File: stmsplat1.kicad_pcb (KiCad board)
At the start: 2 copper layers, 5 parts, among them CN10 Conn_01x34_Male, CN7 Conn_01x20_Male, CN8 Conn_01x16_Male, CN9 Conn_01x30_Male, U1 NUCLEO144-F746ZG

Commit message: Experimented with KiCad operations
Tried new symbols  / footprints etc
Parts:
- added J1: Conn_Coaxial, Connector_Coaxial:SMB_Jack_Vertical, F.Cu at (61.6, 49.5)
- added J2: Conn_Coaxial, Connector_Coaxial:SMB_Jack_Vertical, F.Cu at (93.3, 59.1)
- added J3: Conn_Coaxial, Connector_Coaxial:SMB_Jack_Vertical, F.Cu at (93.3, 38.1)
- added RN1: R_Pack04, Resistor_SMD:R_Array_Convex_4x1206, F.Cu at (73.4, 61.3)
- added RN2: R_Pack04, Resistor_SMD:R_Array_Convex_4x1206, F.Cu at (82.5, 61.3)
- added U2: SA630D, Package_SO:SOIC-8_3.9x4.9mm_P1.27mm, F.Cu at (81.9, 48.9)

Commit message: minor changes - still experimenting
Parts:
- added CN1: C_Pack04, symbols:C_Array_Convex_4x1206, F.Cu at (111.8, 49.5)
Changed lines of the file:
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@@
     (tracks 0)
     (zones 0)
-    (modules 11)
-    (nets 272)
+    (modules 12)
+    (nets 280)
   )
   (page A4)
@@
   (net 270 "Net-(RN2-Pad4)")
   (net 271 "Net-(RN2-Pad1)")
+  (net 272 "Net-(CN1-Pad1)")
+  (net 273 "Net-(CN1-Pad4)")
+  (net 274 "Net-(CN1-Pad2)")
+  (net 275 "Net-(CN1-Pad3)")
+  (net 276 "Net-(CN1-Pad7)")
+  (net 277 "Net-(CN1-Pad8)")
+  (net 278 "Net-(CN1-Pad5)")
+  (net 279 "Net-(CN1-Pad6)")
   (net_class Default "This is the default net class."
     (clearance 0.2)
@@
     (uvia_dia 0.3)
     (uvia_drill 0.1)
+    (add_net "Net-(CN1-Pad1)")
+    (add_net "Net-(CN1-Pad2)")
+    (add_net "Net-(CN1-Pad3)")
+    (add_net "Net-(CN1-Pad4)")
+    (add_net "Net-(CN1-Pad5)")
+    (add_net "Net-(CN1-Pad6)")
+    (add_net "Net-(CN1-Pad7)")
+    (add_net "Net-(CN1-Pad8)")
     (add_net "Net-(CN10-Pad1)")
     (add_net "Net-(CN10-Pad10)")
@@
     (add_net "Net-(U2-Pad7)")
   )
+  (module symbols:C_Array_Convex_4x1206 (layer F.Cu)
+    (at 111.76 49.53)
+    (descr "Chip Resistor Network, ROHM MNR34 (see mnr_g.pdf)")
+    (tags "resistor array")
+    (attr smd)
+    (fp_text reference CN1 (at 0 -3.5) (layer F.SilkS)
+      (effects (font (size 1 1) (thickness 0.15)))
+    )
+    (fp_text value C_Pack04 (at 0 3.5) (layer F.Fab)
+      (effects (font (size 1 1) (thickness 0.15)))
+    )
+    (fp_text user %R (at 0 0 90) (layer F.Fab)
+      (effects (font (size 0.7 0.7) (thickness 0.105)))
+    )
+    (fp_line (start -1.6 -2.6) (end -1.6 2.6) (layer F.Fab) (width 0.1))
+    (fp_line (start -1.6 2.6) (end 1.6 2.6) (layer F.Fab) (width 0.1))
+    (fp_line (start 1.6 2.6) (end 1.6 -2.6) (layer F.Fab) (width 0.1))
+    (fp_line (start 1.6 -2.6) (end -1.6 -2.6) (layer F.Fab) (width 0.1))
+    (fp_line (start 1.05 2.67) (end -1.05 2.67) (layer F.SilkS) (width 0.12))
+    (fp_line (start 1.05 -2.67) (end -1.05 -2.67) (layer F.SilkS) (width 0.12))
+    (fp_line (start -2.21 -2.85) (end 2.2 -2.85) (layer F.CrtYd) (width 0.05))
+    (fp_line (start -2.21 -2.85) (end -2.21 2.85) (layer F.CrtYd) (width 0.05))
+    (fp_line (start 2.2 2.85) (end 2.2 -2.85) (layer F.CrtYd) (width 0.05))
+    (fp_line (start 2.2 2.85) (end -2.21 2.85) (layer F.CrtYd) (width 0.05))
+    (pad 1 smd rect (at -1.5 -2) (size 0.9 0.9) (layers F.Cu F.Paste F.Mask)
+      (net 272 "Net-(CN1-Pad1)"))
+    (pad 4 smd rect (at -1.5 2) (size 0.9 0.9) (layers F.Cu F.Paste F.Mask)
+      (net 273 "Net-(CN1-Pad4)"))
+    (pad 2 smd rect (at -1.5 -0.66) (size 0.9 0.9) (layers F.Cu F.Paste F.Mask)
+      (net 274 "Net-(CN1-Pad2)"))
+    (pad 3 smd rect (at -1.5 0.66) (size 0.9 0.9) (layers F.Cu F.Paste F.Mask)
+      (net 275 "Net-(CN1-Pad3)"))
+    (pad 7 smd rect (at 1.5 -0.66) (size 0.9 0.9) (layers F.Cu F.Paste F.Mask)
+      (net 276 "Net-(CN1-Pad7)"))
+    (pad 8 smd rect (at 1.5 -2) (size 0.9 0.9) (layers F.Cu F.Paste F.Mask)
+      (net 277 "Net-(CN1-Pad8)"))
+    (pad 5 smd rect (at 1.5 2) (size 0.9 0.9) (layers F.Cu F.Paste F.Mask)
+      (net 278 "Net-(CN1-Pad5)"))
+    (pad 6 smd rect (at 1.5 0.66) (size 0.9 0.9) (layers F.Cu F.Paste F.Mask)
+      (net 279 "Net-(CN1-Pad6)"))
+    (model ${KISYS3DMOD}/Resistor_SMD.3dshapes/R_Array_Convex_4x1206.wrl
+      (at (xyz 0 0 0))
+      (scale (xyz 1 1 1))
+      (rotate (xyz 0 0 0))
+    )
+  )
   (module Resistor_SMD:R_Array_Convex_4x1206 (layer F.Cu)

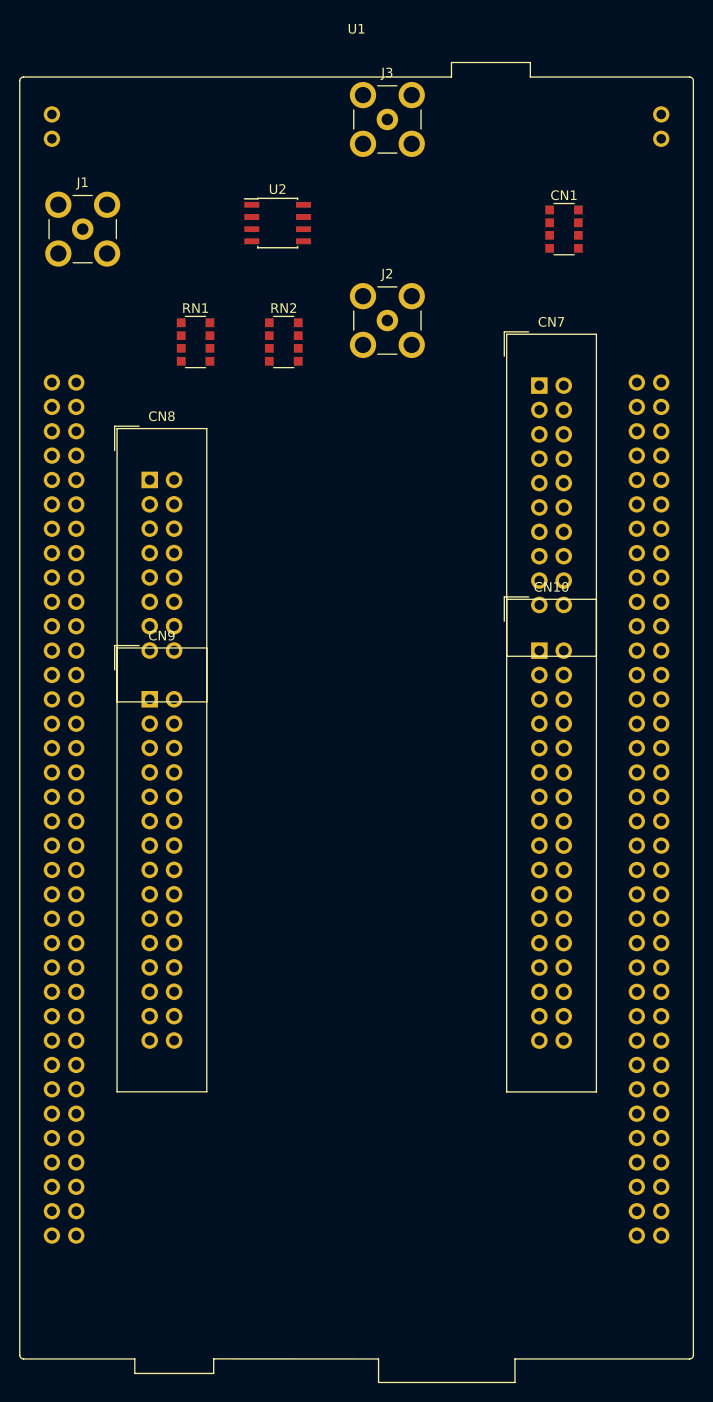
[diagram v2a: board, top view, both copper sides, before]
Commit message: pcb outline and start trim of connectors
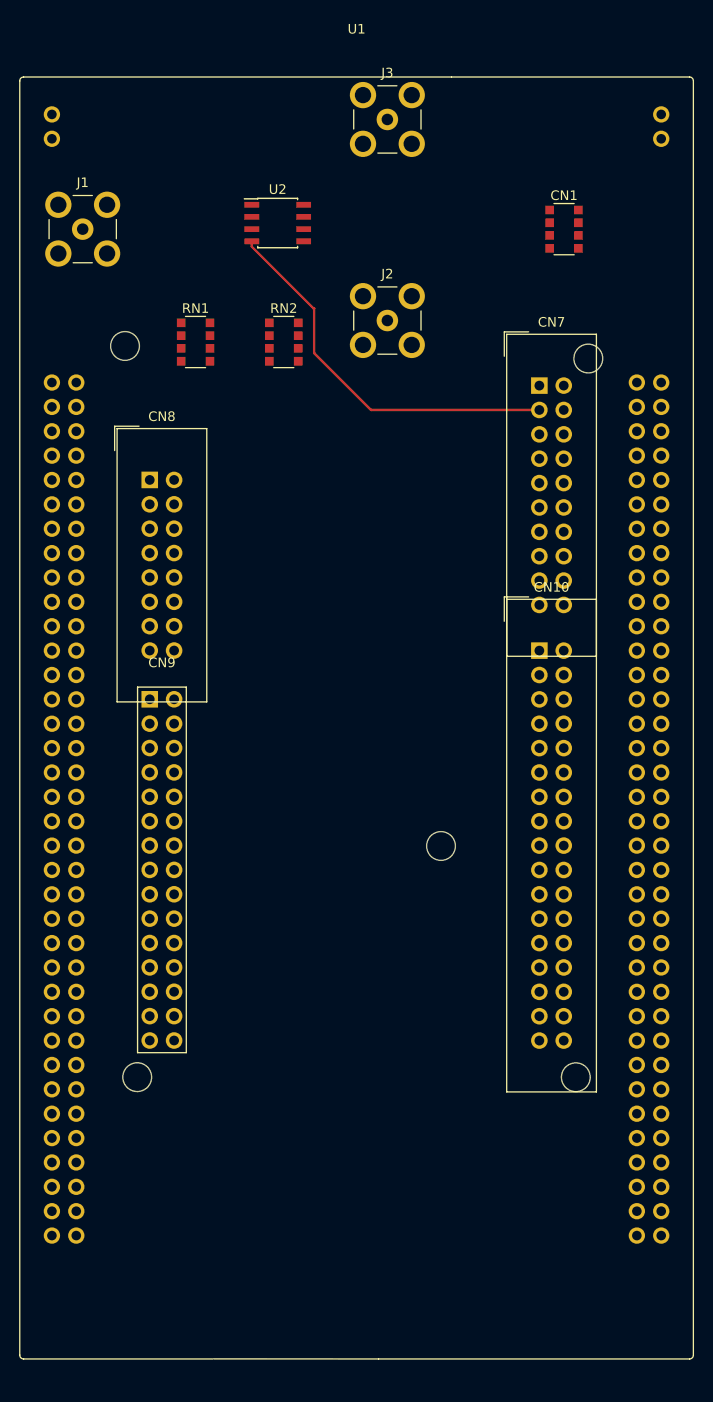
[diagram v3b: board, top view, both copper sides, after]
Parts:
- CN9: footprint Connector_IDC:IDC-Header_2x15_P2.54mm_Vertical -> symbols:IDC-Pins_2x15_P2.54mm_Vertical
- U1: footprint Module:ST_Morpho_Connector_144_STLink -> symbols:ST_Nucleo_144_Large_Daughter
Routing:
- net /PB15: track 0.00 -> 40.3 mm

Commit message: Getting ready for proper start to project
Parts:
- added U3: MCP6S93-X_UN, spatboard:MCP6S93-X&slash_UN, F.Cu at (95.9, 48.3)
- CN1: value C_Pack04 -> C_Pack04-c_pack04; footprint symbols:C_Array_Convex_4x1206 -> spatboard:C_Array_Convex_5x1206
- CN10: footprint Connector_IDC:IDC-Header_2x17_P2.54mm_Vertical -> spatboard:IDC-Pins_2x17_P2.54mm_Vertical
- CN7: footprint Connector_IDC:IDC-Header_2x10_P2.54mm_Vertical -> spatboard:IDC-Pins_2x10_P2.54mm_Vertical
- CN8: footprint Connector_IDC:IDC-Header_2x08_P2.54mm_Vertical -> spatboard:IDC-Pins_2x8_P2.54mm_Vertical
- U2: value SA630D -> SA630D-RF_Switch

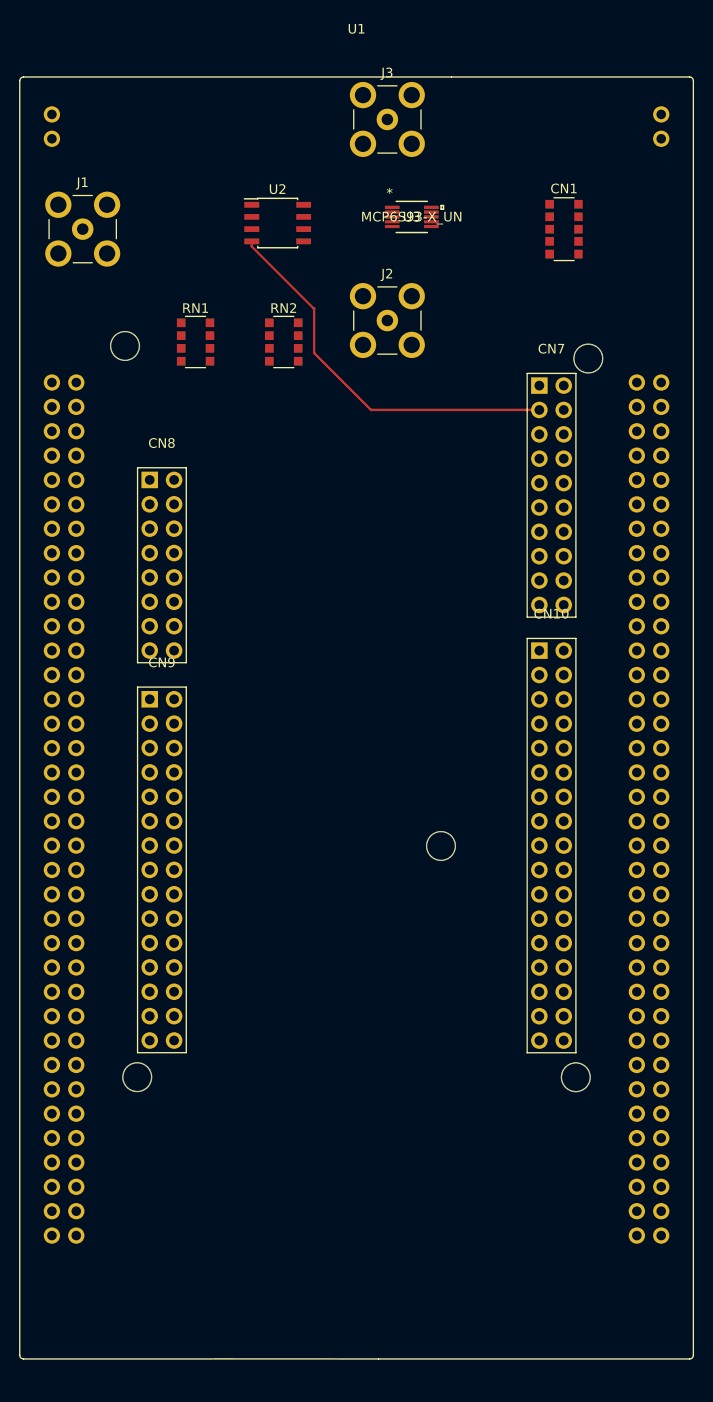
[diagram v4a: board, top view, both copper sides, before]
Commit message: Arduino connectors moved to correct position
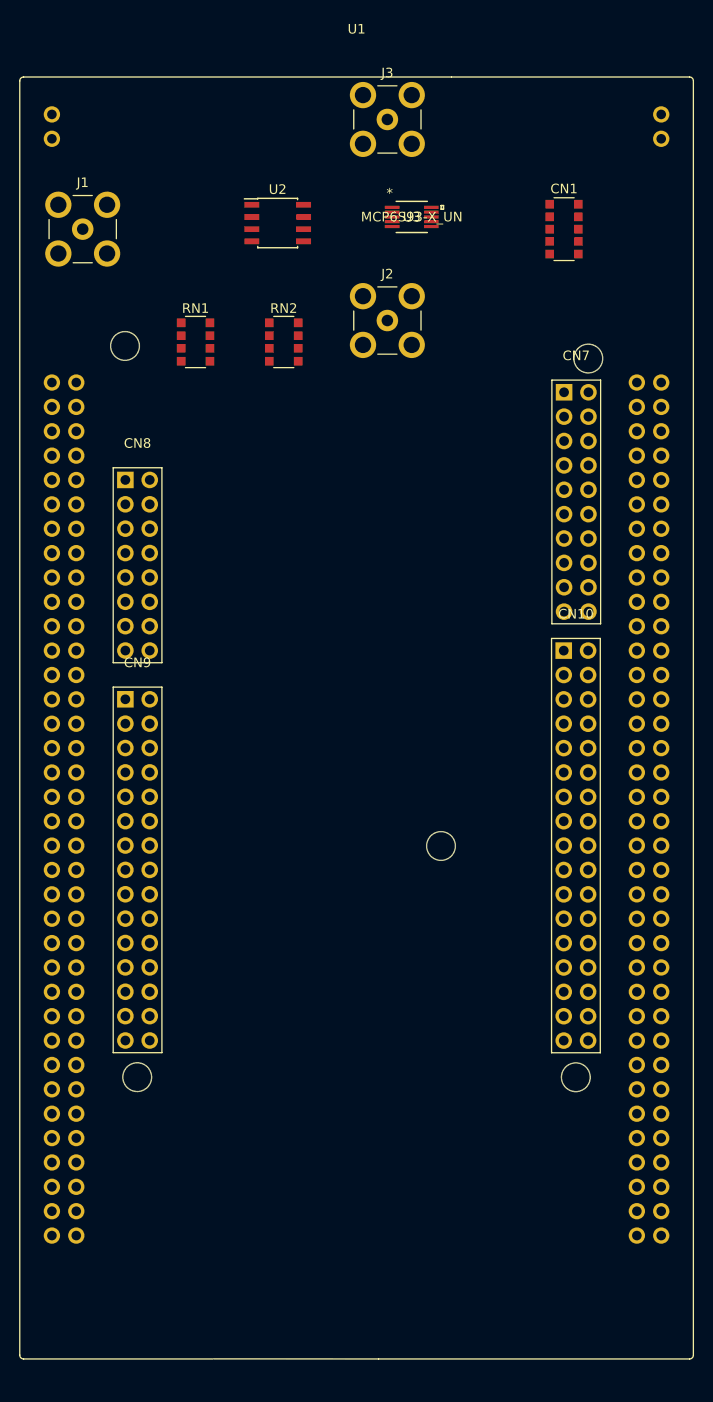
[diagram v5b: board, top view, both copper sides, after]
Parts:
- moved CN7 2.67 mm to (111.8, 66.5)
- moved CN10 2.54 mm to (111.7, 93.5)
- moved CN8 2.54 mm to (66.0, 75.7)
- moved CN9 2.54 mm to (66.0, 98.5)
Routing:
- net /PB15: track 40.3 -> 0.00 mm

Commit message: Cropped PCB to clear STM board buttons
Added GPS module connector and silkscreen
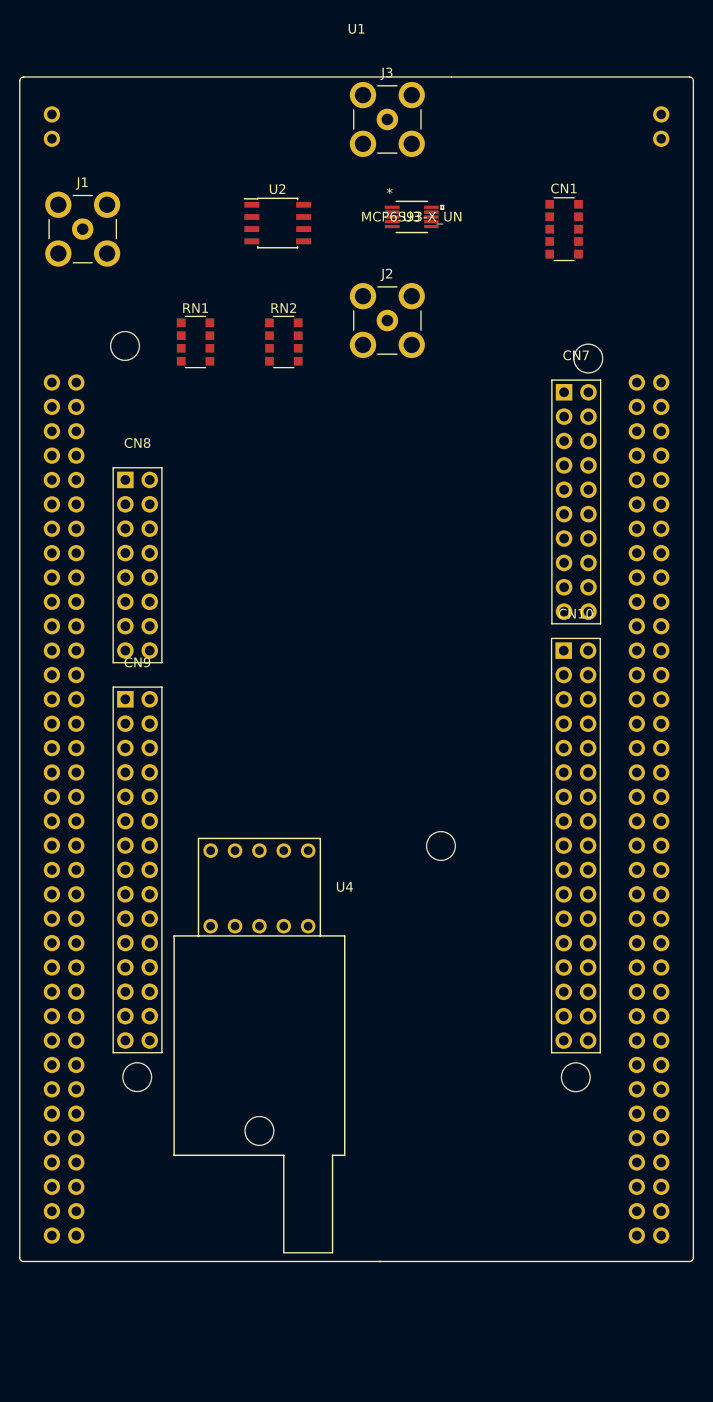
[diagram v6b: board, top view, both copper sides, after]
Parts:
- added U4: ublox_SAM-M8Q, spatboard:GPS_IDC-Header_2x05_P2.54mm_Horizontal, F.Cu at (85.1, 114.3)
- CN9: footprint symbols:IDC-Pins_2x15_P2.54mm_Vertical -> spatboard:IDC-Pins_2x15_P2.54mm_Vertical
- U1: footprint symbols:ST_Nucleo_144_Large_Daughter -> spatboard:ST_Nucleo_144_Large_Daughter

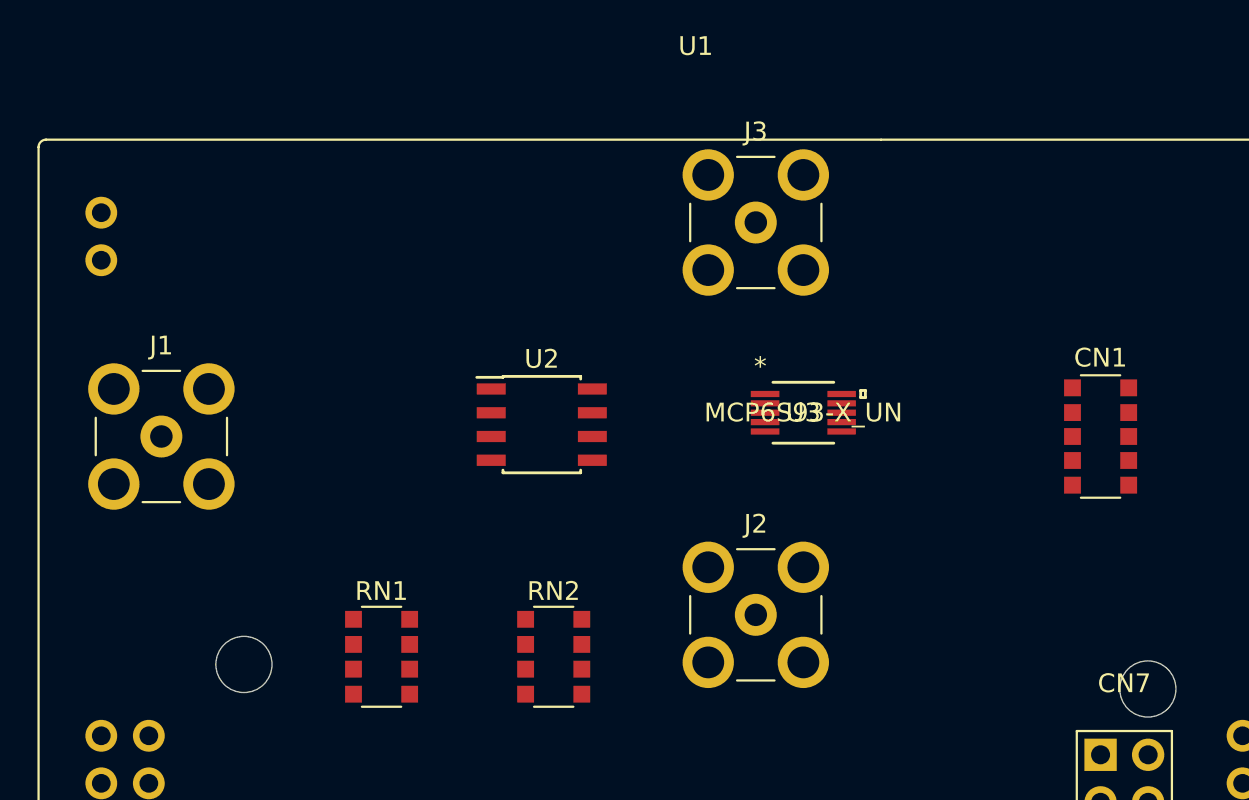
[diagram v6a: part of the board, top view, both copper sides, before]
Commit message: Footprints re-assigned
PCB had lost associations
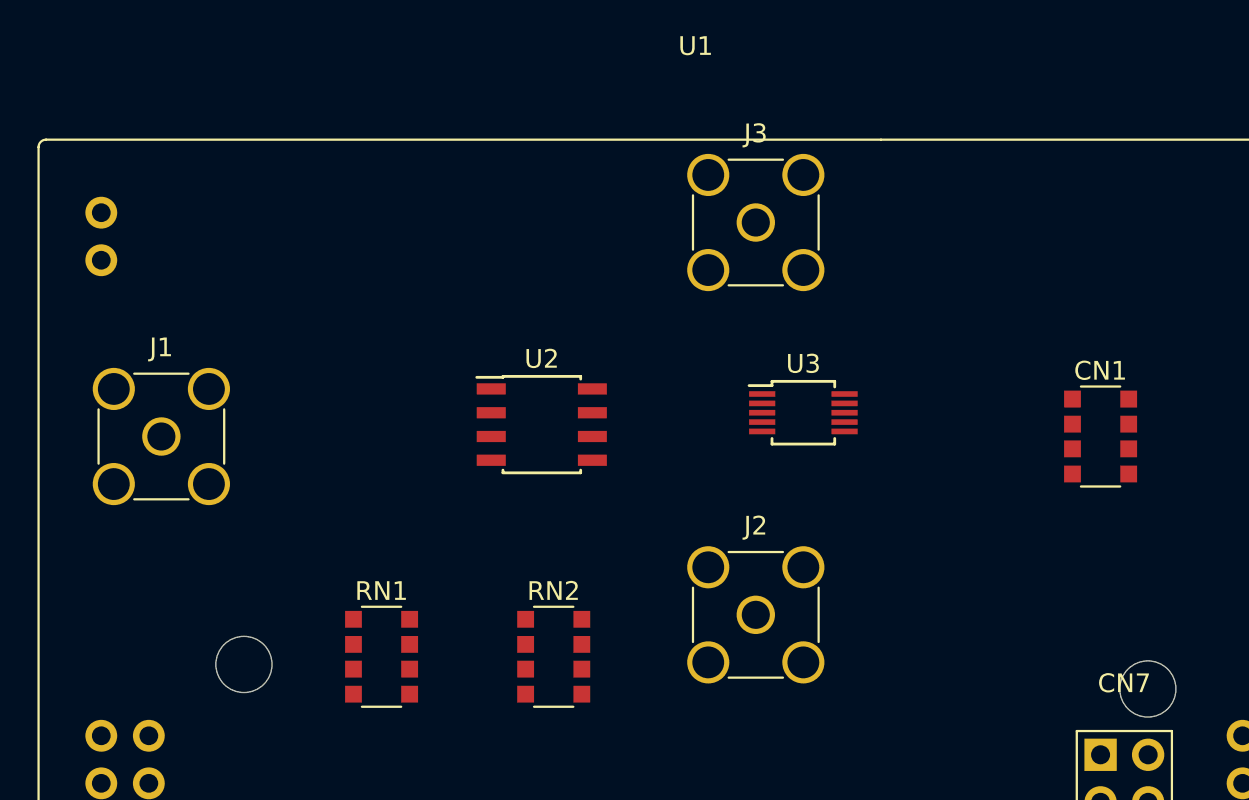
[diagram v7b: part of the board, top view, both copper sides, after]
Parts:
- CN1: value C_Pack04-c_pack04 -> C_Pack04; footprint spatboard:C_Array_Convex_5x1206 -> spatboard:C_Array_Convex_4x1206
- J1, J2, J3: footprint Connector_Coaxial:SMB_Jack_Vertical -> Connector_Coaxial:SMA_Amphenol_132134-11_Vertical
- U3: footprint spatboard:MCP6S93-X&slash_UN -> Package_SO:MSOP-10_3x3mm_P0.5mm
- U4: value ublox_SAM-M8Q -> ublox_chinese_PCB_module
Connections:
- net Net-(CN8-Pad10) renamed /PC12
- net Net-(CN8-Pad11) renamed /GND
- net Net-(CN8-Pad12) renamed /PD2
- net Net-(CN8-Pad14) renamed /PG2
- net Net-(CN8-Pad15) renamed /VIN
- net Net-(CN8-Pad16) renamed /PG3
- net Net-(CN8-Pad2) renamed /PC8
- net Net-(CN8-Pad3) renamed /IOREF
- net Net-(CN8-Pad4) renamed /PC9
- net Net-(CN8-Pad5) renamed /RESET
- net Net-(CN8-Pad6) renamed /PC10
- net Net-(CN8-Pad7) renamed /+3V3
- net Net-(CN8-Pad8) renamed /PC11
- net Net-(CN8-Pad9) renamed /+5V
- U3 pad 5: Net-(J1-Pad2) -> Net-(U3-Pad5)
